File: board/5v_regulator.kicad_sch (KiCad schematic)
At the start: 10 parts, among them U601 TPS61023

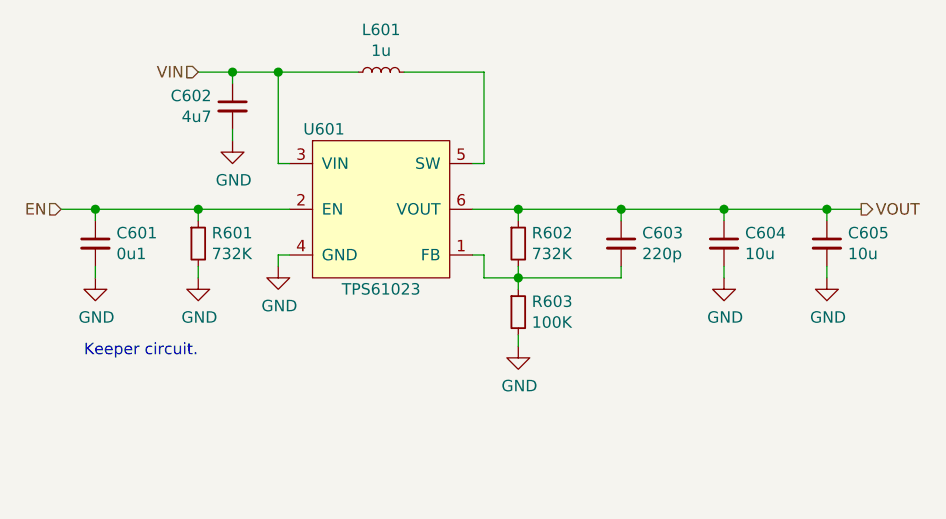
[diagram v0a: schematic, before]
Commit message: Added testpoints and other fixes
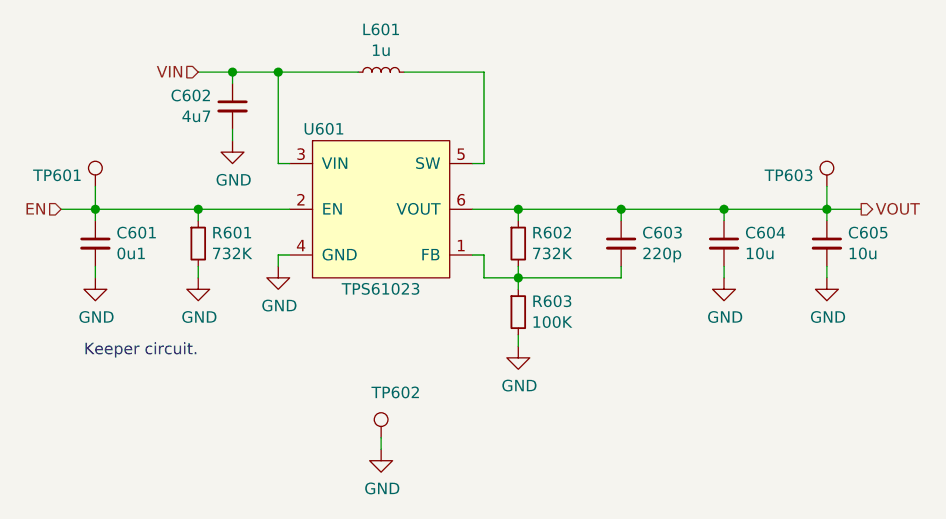
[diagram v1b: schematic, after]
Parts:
- added TP601, TP602, TP603: TestPoint, DIYPie:TestPoint_Pad_D1.5mm, symbol DIYPie:TestPoint
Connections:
- net EN: now also TP601.1
- net GND: now also TP602.1
- net VOUT: now also TP603.1
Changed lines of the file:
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@@
+    (stroke (width 0) (type solid) (color 0 0 0 0))
+  )
+  (wire (pts (xy 113.03 95.25) (xy 113.03 97.79))
     (stroke (width 0) (type solid) (color 0 0 0 0))
   )
@@
     (stroke (width 0) (type solid) (color 0 0 0 0))
   )
+  (wire (pts (xy 144.78 123.19) (xy 144.78 124.46))
+    (stroke (width 0) (type solid) (color 0 0 0 0))
+  )
   (wire (pts (xy 154.94 92.71) (xy 156.21 92.71))
     (stroke (width 0) (type solid) (color 0 0 0 0))
@@
   )
   (wire (pts (xy 182.88 105.41) (xy 182.88 104.14))
+    (stroke (width 0) (type solid) (color 0 0 0 0))
+  )
+  (wire (pts (xy 194.31 95.25) (xy 194.31 97.79))
     (stroke (width 0) (type solid) (color 0 0 0 0))
   )
@@
   (hierarchical_label "VOUT" (shape output) (at 198.12 97.79 0)
     (effects (font (size 1.27 1.27)) (justify left))
+  )
+  (symbol (lib_id "DIYPie:TestPoint") (at 113.03 95.25 0) (mirror y) (unit 1)
+    (in_bom yes) (on_board yes)
+    (property "Reference" "TP601" (id 0) (at 111.5568 94.0562 0)
+      (effects (font (size 1.27 1.27)) (justify left))
+    )
+    (property "Value" "TestPoint" (id 1) (at 111.5568 95.1992 0)
+      (effects (font (size 1.27 1.27)) (justify left) hide)
+    )
+    (property "Footprint" "DIYPie:TestPoint_Pad_D1.5mm" (id 2) (at 107.95 95.25 0)
+      (effects (font (size 1.27 1.27)) hide)
+    )
+    (property "Datasheet" "~" (id 3) (at 107.95 95.25 0)
+      (effects (font (size 1.27 1.27)) hide)
+    )
+    (property "Description" "Generic testpoint" (id 4) (at 113.03 95.25 0)
+      (effects (font (size 1.27 1.27)) hide)
+    )
+    (property "Manufacturer" "~" (id 5) (at 113.03 95.25 0)
+      (effects (font (size 1.27 1.27)) hide)
+    )
+    (property "Manufacturer_PN" "~" (id 6) (at 113.03 95.25 0)
+      (effects (font (size 1.27 1.27)) hide)
+    )
+    (property "Mouser_PN" "~" (id 7) (at 113.03 95.25 0)
+      (effects (font (size 1.27 1.27)) hide)
+    )
+    (property "Mouser_PL" "~" (id 8) (at 113.03 95.25 0)
+      (effects (font (size 1.27 1.27)) hide)
+    )
+    (property "LCSC_PN" "~" (id 9) (at 113.03 95.25 0)
+      (effects (font (size 1.27 1.27)) hide)
+    )
+    (property "LCSC_PL" "~" (id 10) (at 113.03 95.25 0)
+      (effects (font (size 1.27 1.27)) hide)
+    )
+    (property "Digikey_PN" "~" (id 11) (at 113.03 95.25 0)
+      (effects (font (size 1.27 1.27)) hide)
+    )
+    (property "Digikey_PL" "~" (id 12) (at 113.03 95.25 0)
+      (effects (font (size 1.27 1.27)) hide)
+    )
+    (property "Other_PN" "~" (id 13) (at 113.03 95.25 0)
+      (effects (font (size 1.27 1.27)) hide)
+    )
+    (property "Other_PL" "~" (id 14) (at 113.03 95.25 0)
+      (effects (font (size 1.27 1.27)) hide)
+    )
+    (property "MOQ" "~" (id 15) (at 113.03 95.25 0)
+      (effects (font (size 1.27 1.27)) hide)
+    )
+    (property "Lead_time" "~" (id 16) (at 113.03 95.25 0)
+      (effects (font (size 1.27 1.27)) hide)
+    )
+    (property "Tolerance" "~" (id 17) (at 113.03 95.25 0)
+      (effects (font (size 1.27 1.27)) hide)
+    )
+    (property "Voltage" "~" (id 18) (at 113.03 95.25 0)
+      (effects (font (size 1.27 1.27)) hide)
+    )
+    (property "Current" "~" (id 19) (at 113.03 95.25 0)
+      (effects (font (size 1.27 1.27)) hide)
+    )
+    (property "Dielectric" "~" (id 20) (at 113.03 95.25 0)
+      (effects (font (size 1.27 1.27)) hide)
+    )
+    (pin "1")
+  )
+  (symbol (lib_id "DIYPie:TestPoint") (at 144.78 123.19 0) (unit 1)
+    (in_bom yes) (on_board yes)
+    (property "Reference" "TP602" (id 0) (at 143.7132 118.1862 0)
+      (effects (font (size 1.27 1.27)) (justify left))
+    )
+    (property "Value" "TestPoint" (id 1) (at 146.2532 123.1392 0)
+      (effects (font (size 1.27 1.27)) (justify left) hide)
+    )
+    (property "Footprint" "DIYPie:TestPoint_Pad_D1.5mm" (id 2) (at 149.86 123.19 0)
+      (effects (font (size 1.27 1.27)) hide)
+    )
+    (property "Datasheet" "~" (id 3) (at 149.86 123.19 0)
+      (effects (font (size 1.27 1.27)) hide)
+    )
+    (property "Description" "Generic testpoint" (id 4) (at 144.78 123.19 0)
+      (effects (font (size 1.27 1.27)) hide)
+    )
+    (property "Manufacturer" "~" (id 5) (at 144.78 123.19 0)
+      (effects (font (size 1.27 1.27)) hide)
+    )
+    (property "Manufacturer_PN" "~" (id 6) (at 144.78 123.19 0)
+      (effects (font (size 1.27 1.27)) hide)
+    )
+    (property "Mouser_PN" "~" (id 7) (at 144.78 123.19 0)
+      (effects (font (size 1.27 1.27)) hide)
+    )
+    (property "Mouser_PL" "~" (id 8) (at 144.78 123.19 0)
+      (effects (font (size 1.27 1.27)) hide)
+    )
+    (property "LCSC_PN" "~" (id 9) (at 144.78 123.19 0)
+      (effects (font (size 1.27 1.27)) hide)
+    )
+    (property "LCSC_PL" "~" (id 10) (at 144.78 123.19 0)
+      (effects (font (size 1.27 1.27)) hide)
+    )
+    (property "Digikey_PN" "~" (id 11) (at 144.78 123.19 0)
+      (effects (font (size 1.27 1.27)) hide)
+    )
+    (property "Digikey_PL" "~" (id 12) (at 144.78 123.19 0)
+      (effects (font (size 1.27 1.27)) hide)
+    )
+    (property "Other_PN" "~" (id 13) (at 144.78 123.19 0)
+      (effects (font (size 1.27 1.27)) hide)
+    )
+    (property "Other_PL" "~" (id 14) (at 144.78 123.19 0)
+      (effects (font (size 1.27 1.27)) hide)
+    )
+    (property "MOQ" "~" (id 15) (at 144.78 123.19 0)
+      (effects (font (size 1.27 1.27)) hide)
+    )
+    (property "Lead_time" "~" (id 16) (at 144.78 123.19 0)
+      (effects (font (size 1.27 1.27)) hide)
+    )
+    (property "Tolerance" "~" (id 17) (at 144.78 123.19 0)
+      (effects (font (size 1.27 1.27)) hide)
+    )
+    (property "Voltage" "~" (id 18) (at 144.78 123.19 0)
+      (effects (font (size 1.27 1.27)) hide)
+    )
+    (property "Current" "~" (id 19) (at 144.78 123.19 0)
+      (effects (font (size 1.27 1.27)) hide)
+    )
+    (property "Dielectric" "~" (id 20) (at 144.78 123.19 0)
+      (effects (font (size 1.27 1.27)) hide)
+    )
+    (pin "1")
+  )
+  (symbol (lib_id "DIYPie:TestPoint") (at 194.31 95.25 0) (mirror y) (unit 1)
+    (in_bom yes) (on_board yes)
+    (property "Reference" "TP603" (id 0) (at 192.8368 94.0562 0)
+      (effects (font (size 1.27 1.27)) (justify left))
+    )
+    (property "Value" "TestPoint" (id 1) (at 192.8368 95.1992 0)
+      (effects (font (size 1.27 1.27)) (justify left) hide)
+    )
+    (property "Footprint" "DIYPie:TestPoint_Pad_D1.5mm" (id 2) (at 189.23 95.25 0)
+      (effects (font (size 1.27 1.27)) hide)
+    )
+    (property "Datasheet" "~" (id 3) (at 189.23 95.25 0)
+      (effects (font (size 1.27 1.27)) hide)
+    )
+    (property "Description" "Generic testpoint" (id 4) (at 194.31 95.25 0)
+      (effects (font (size 1.27 1.27)) hide)
+    )
+    (property "Manufacturer" "~" (id 5) (at 194.31 95.25 0)
+      (effects (font (size 1.27 1.27)) hide)
+    )
+    (property "Manufacturer_PN" "~" (id 6) (at 194.31 95.25 0)
+      (effects (font (size 1.27 1.27)) hide)
+    )
+    (property "Mouser_PN" "~" (id 7) (at 194.31 95.25 0)
+      (effects (font (size 1.27 1.27)) hide)
+    )
+    (property "Mouser_PL" "~" (id 8) (at 194.31 95.25 0)
+      (effects (font (size 1.27 1.27)) hide)
+    )
+    (property "LCSC_PN" "~" (id 9) (at 194.31 95.25 0)
+      (effects (font (size 1.27 1.27)) hide)
+    )
+    (property "LCSC_PL" "~" (id 10) (at 194.31 95.25 0)
+      (effects (font (size 1.27 1.27)) hide)
+    )
+    (property "Digikey_PN" "~" (id 11) (at 194.31 95.25 0)
+      (effects (font (size 1.27 1.27)) hide)
+    )
+    (property "Digikey_PL" "~" (id 12) (at 194.31 95.25 0)
+      (effects (font (size 1.27 1.27)) hide)
+    )
+    (property "Other_PN" "~" (id 13) (at 194.31 95.25 0)
+      (effects (font (size 1.27 1.27)) hide)
+    )
+    (property "Other_PL" "~" (id 14) (at 194.31 95.25 0)
+      (effects (font (size 1.27 1.27)) hide)
+    )
+    (property "MOQ" "~" (id 15) (at 194.31 95.25 0)
+      (effects (font (size 1.27 1.27)) hide)
+    )
+    (property "Lead_time" "~" (id 16) (at 194.31 95.25 0)
+      (effects (font (size 1.27 1.27)) hide)
+    )
+    (property "Tolerance" "~" (id 17) (at 194.31 95.25 0)
+      (effects (font (size 1.27 1.27)) hide)
+    )
+    (property "Voltage" "~" (id 18) (at 194.31 95.25 0)
+      (effects (font (size 1.27 1.27)) hide)
+    )
+    (property "Current" "~" (id 19) (at 194.31 95.25 0)
+      (effects (font (size 1.27 1.27)) hide)
+    )
+    (property "Dielectric" "~" (id 20) (at 194.31 95.25 0)
+      (effects (font (size 1.27 1.27)) hide)
+    )
+    (pin "1")
   )
   (symbol (lib_id "Device:L_Small") (at 144.78 82.55 90) (unit 1)
@@
     (pin "1")
   )
+  (symbol (lib_id "power:GND") (at 144.78 124.46 0) (unit 1)
+    (in_bom yes) (on_board yes)
+    (property "Reference" "#PWR0605" (id 0) (at 144.78 130.81 0)
+      (effects (font (size 1.27 1.27)) hide)
+    )
+    (property "Value" "GND" (id 1) (at 144.907 128.8542 0))
+    (property "Footprint" "" (id 2) (at 144.78 124.46 0)
+      (effects (font (size 1.27 1.27)) hide)
+    )
+    (property "Datasheet" "" (id 3) (at 144.78 124.46 0)
+      (effects (font (size 1.27 1.27)) hide)
+    )
+    (pin "1")
+  )
   (symbol (lib_id "power:GND") (at 160.02 113.03 0) (unit 1)
     (in_bom yes) (on_board yes)
-    (property "Reference" "#PWR0605" (id 0) (at 160.02 119.38 0)
+    (property "Reference" "#PWR0606" (id 0) (at 160.02 119.38 0)
       (effects (font (size 1.27 1.27)) hide)
     )
@@
   (symbol (lib_id "power:GND") (at 182.88 105.41 0) (unit 1)
     (in_bom yes) (on_board yes)
-    (property "Reference" "#PWR0606" (id 0) (at 182.88 111.76 0)
+    (property "Reference" "#PWR0607" (id 0) (at 182.88 111.76 0)
       (effects (font (size 1.27 1.27)) hide)
     )
@@
   (symbol (lib_id "power:GND") (at 194.31 105.41 0) (unit 1)
     (in_bom yes) (on_board yes)
-    (property "Reference" "#PWR0607" (id 0) (at 194.31 111.76 0)
-      (effects (font (size 1.27 1.27)) hide)
-    )
+    (property "Reference" "#PWR0608" (id 0) (at 194.31 111.76 0)
+      (effects (font (size 1.27 1.27)) hide)
+    )
